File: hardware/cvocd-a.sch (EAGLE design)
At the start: 78 parts, among them IC1 6N138, IC2 LM324D, IC3 MCP4728_QUAD_DAC, IC4 REG1117, IC5 PIC16F1825SO14, IC6 74HC595D, IC7 74HC595D

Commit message: v5 pcb release candidate
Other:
- note added: "REVISION 5, 22 FEB 2018"
- note removed: "REVISION 4, 30 JAN 2018"
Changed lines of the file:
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@@
 <plain>
 <text x="59.436" y="172.212" size="3.81" layer="95">CV.OCD MIDI TO CV CONVERTER</text>
-<text x="59.944" y="166.37" size="3.81" layer="95">REVISION 4, 30 JAN 2018</text>
+<text x="59.944" y="166.37" size="3.81" layer="95">REVISION 5, 22 FEB 2018</text>
 <text x="59.944" y="160.782" size="3.81" layer="95">Jason Hotchkiss, Sixty-Four Pixels Ltd</text>
 <text x="-152.4" y="185.42" size="3.81" layer="95">POWER SUPPLY</text>
@@
 <wire x1="137.16" y1="114.3" x2="147.32" y2="114.3" width="0.1524" layer="91"/>
 <junction x="137.16" y="114.3"/>
+<junction x="147.32" y="114.3"/>
 </segment>
 </net>
@@
 <wire x1="137.16" y1="99.06" x2="147.32" y2="99.06" width="0.1524" layer="91"/>
 <junction x="137.16" y="99.06"/>
+<junction x="147.32" y="99.06"/>
 </segment>
 </net>
@@
 <wire x1="137.16" y1="83.82" x2="147.32" y2="83.82" width="0.1524" layer="91"/>
 <junction x="137.16" y="83.82"/>
+<junction x="147.32" y="83.82"/>
 </segment>
 </net>
@@
 <wire x1="137.16" y1="68.58" x2="147.32" y2="68.58" width="0.1524" layer="91"/>
 <junction x="137.16" y="68.58"/>
+<junction x="147.32" y="68.58"/>
 </segment>
 </net>
@@
 <wire x1="162.56" y1="106.68" x2="162.56" y2="114.3" width="0.1524" layer="91"/>
 <junction x="162.56" y="114.3"/>
+<junction x="157.48" y="114.3"/>
+<junction x="157.48" y="106.68"/>
 </segment>
 </net>
@@
 <wire x1="162.56" y1="91.44" x2="162.56" y2="99.06" width="0.1524" layer="91"/>
 <junction x="162.56" y="99.06"/>
+<junction x="157.48" y="99.06"/>
+<junction x="157.48" y="91.44"/>
 </segment>
 </net>
@@
 <wire x1="162.56" y1="76.2" x2="162.56" y2="83.82" width="0.1524" layer="91"/>
 <junction x="162.56" y="83.82"/>
+<junction x="157.48" y="83.82"/>
+<junction x="157.48" y="76.2"/>
 </segment>
 </net>
@@
 <wire x1="162.56" y1="60.96" x2="162.56" y2="68.58" width="0.1524" layer="91"/>
 <junction x="162.56" y="68.58"/>
-</segment>
-</net>
+<junction x="157.48" y="68.58"/>
+<junction x="157.48" y="60.96"/>
+</segment>
+</net>

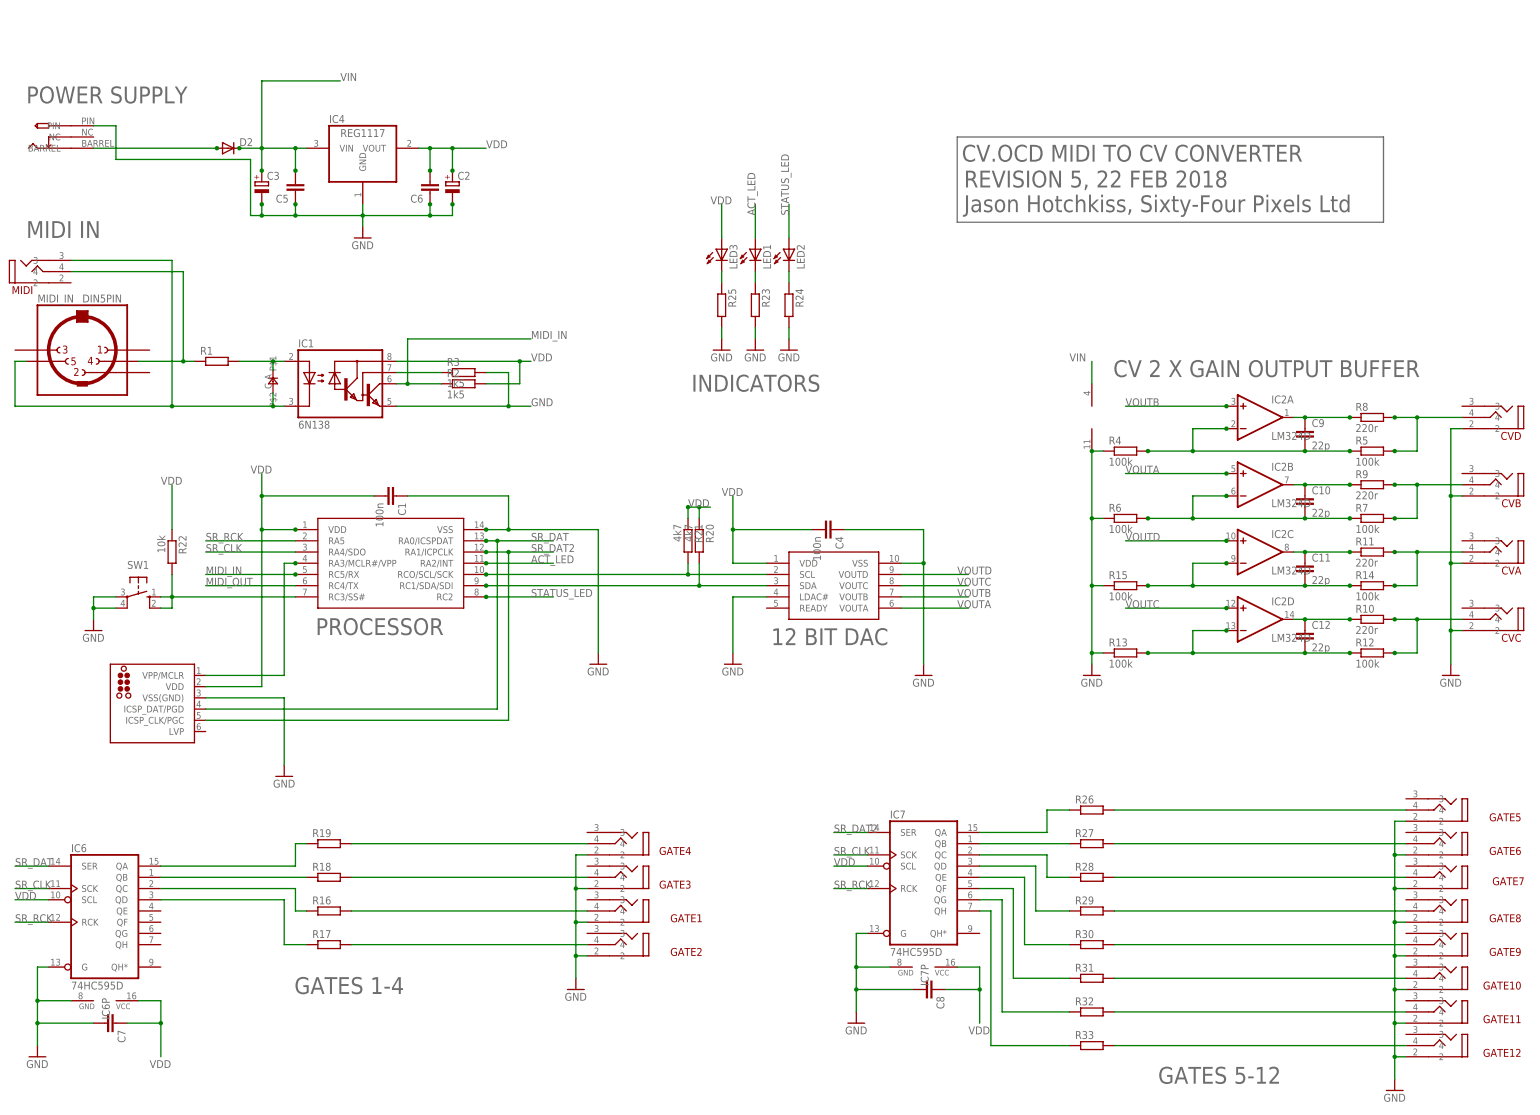
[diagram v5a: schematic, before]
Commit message: V5.1 SILK SCREEN UPDATES
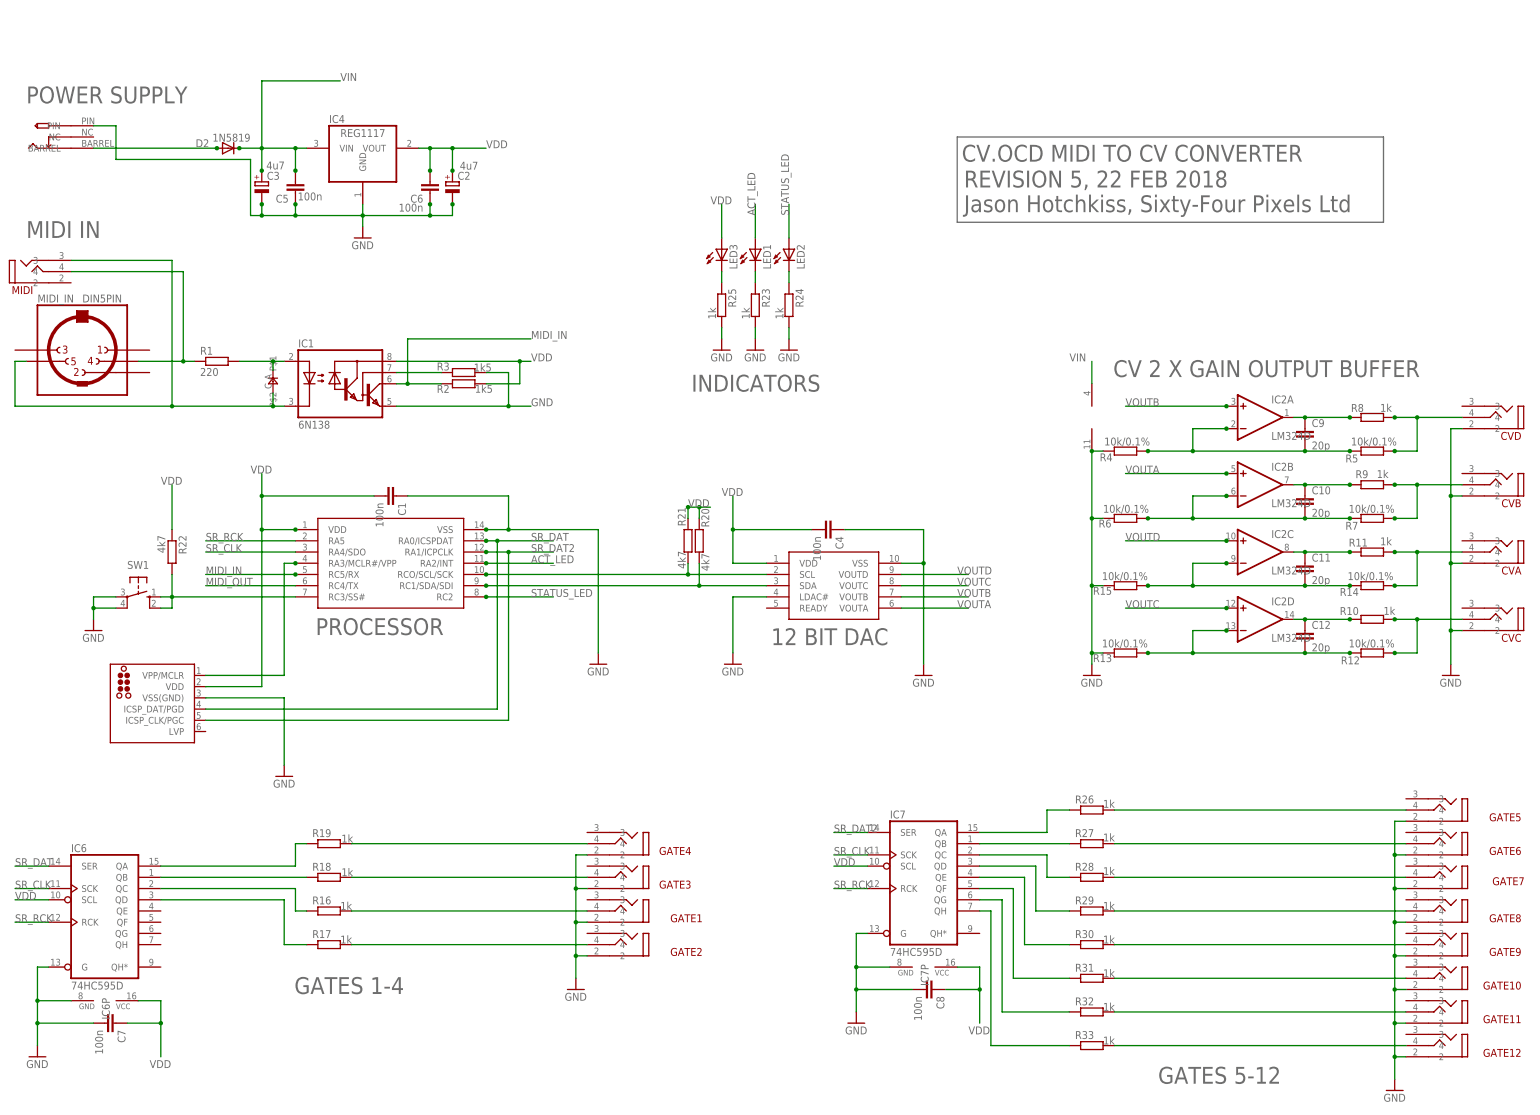
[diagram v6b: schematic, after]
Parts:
- C10, C11, C12, C9: value 22p -> 20p
- C2, C3: value (none) -> 4u7
- C5, C6, C7, C8: value (none) -> 100n
- D2: value (none) -> 1N5819
- R1: value (none) -> 220
- R10, R11, R8, R9: value 220r -> 1k
- R12, R13, R14, R15, R4, R5, R6, R7: value 100k -> 10k/0.1%
- R16, R17, R18, R19, R23, R24, R25, R26, R27, R28, R29, R30, R31, R32, R33: value (none) -> 1k
- R22: value 10k -> 4k7

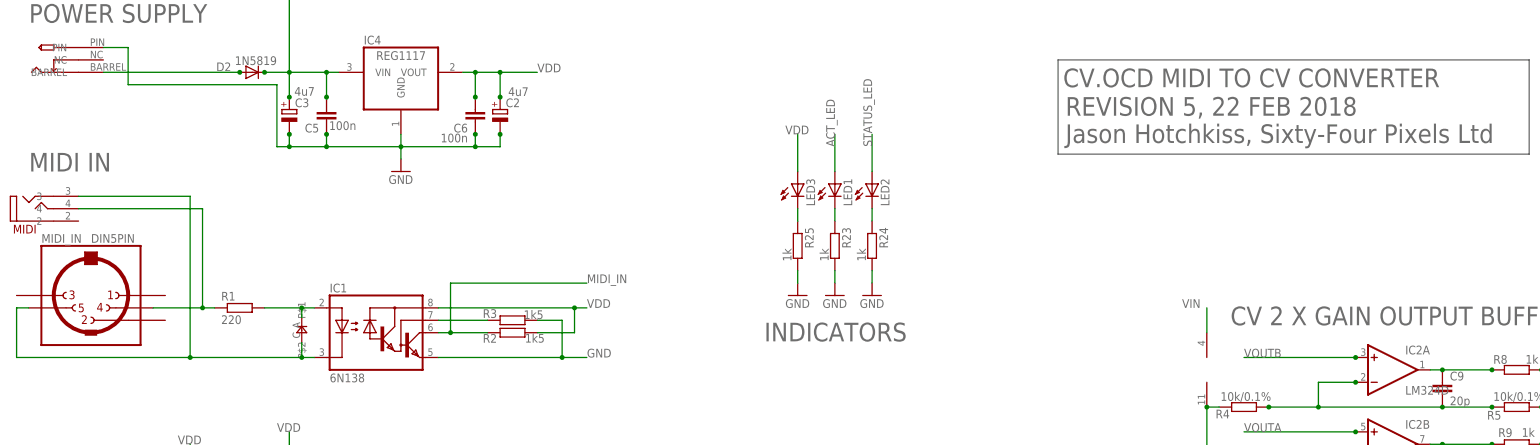
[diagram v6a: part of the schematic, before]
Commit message: V6 candidate
change polarity on mini midi in socket
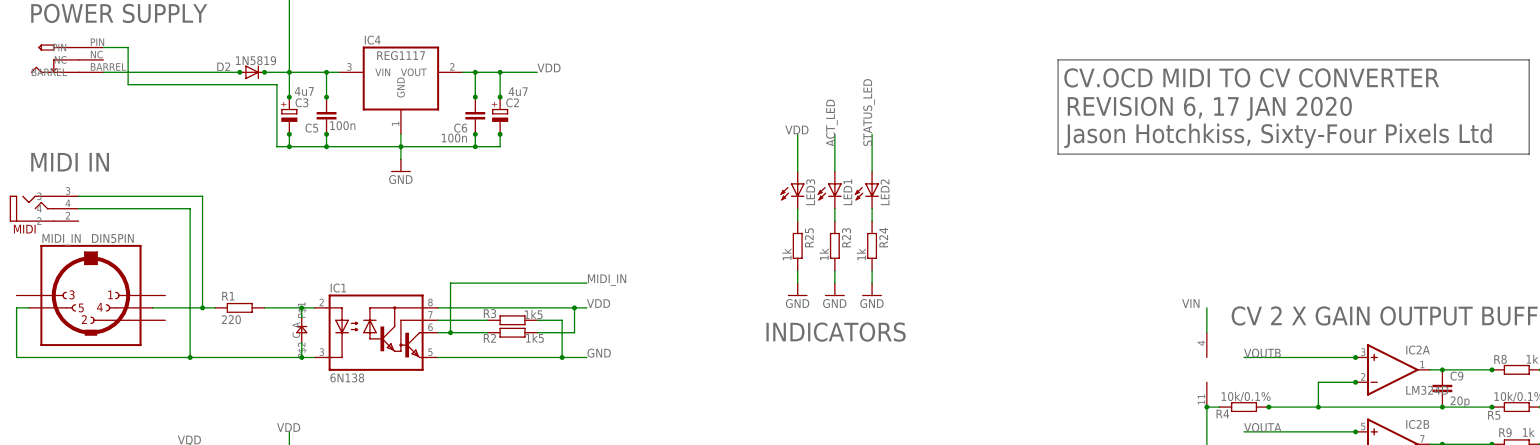
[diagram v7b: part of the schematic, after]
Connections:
- net N$29: now also MIDI.3; no longer MIDI.4
- net N$31: now also MIDI.4; no longer MIDI.3
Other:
- note added: "REVISION 6, 17 JAN 2020"
- note removed: "REVISION 5, 22 FEB 2018"
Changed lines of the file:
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@@
 <plain>
 <text x="59.436" y="172.212" size="3.81" layer="95">CV.OCD MIDI TO CV CONVERTER</text>
-<text x="59.944" y="166.37" size="3.81" layer="95">REVISION 5, 22 FEB 2018</text>
+<text x="59.944" y="166.37" size="3.81" layer="95">REVISION 6, 17 JAN 2020</text>
 <text x="59.944" y="160.782" size="3.81" layer="95">Jason Hotchkiss, Sixty-Four Pixels Ltd</text>
 <text x="-152.4" y="185.42" size="3.81" layer="95">POWER SUPPLY</text>
@@
 <pinref part="R1" gate="G$1" pin="1"/>
 <wire x1="-127" y1="127" x2="-116.84" y2="127" width="0.1524" layer="91"/>
-<pinref part="MIDI" gate="G$1" pin="4"/>
 <wire x1="-116.84" y1="127" x2="-114.3" y2="127" width="0.1524" layer="91"/>
-<wire x1="-142.24" y1="147.32" x2="-116.84" y2="147.32" width="0.1524" layer="91"/>
-<wire x1="-116.84" y1="147.32" x2="-116.84" y2="127" width="0.1524" layer="91"/>
+<wire x1="-116.84" y1="149.86" x2="-116.84" y2="127" width="0.1524" layer="91"/>
 <junction x="-116.84" y="127"/>
+<pinref part="MIDI" gate="G$1" pin="3"/>
+<wire x1="-142.24" y1="149.86" x2="-116.84" y2="149.86" width="0.1524" layer="91"/>
 </segment>
 </net>
@@
 <wire x1="-96.52" y1="119.888" x2="-96.52" y2="116.84" width="0.1524" layer="91"/>
 <junction x="-96.52" y="116.84"/>
-<pinref part="MIDI" gate="G$1" pin="3"/>
-<wire x1="-142.24" y1="149.86" x2="-119.38" y2="149.86" width="0.1524" layer="91"/>
-<wire x1="-119.38" y1="149.86" x2="-119.38" y2="116.84" width="0.1524" layer="91"/>
+<wire x1="-119.38" y1="147.32" x2="-119.38" y2="116.84" width="0.1524" layer="91"/>
 <junction x="-119.38" y="116.84"/>
-</segment>
-</net>
+<pinref part="MIDI" gate="G$1" pin="4"/>
+<wire x1="-142.24" y1="147.32" x2="-119.38" y2="147.32" width="0.1524" layer="91"/>
+</segment>
+</net>

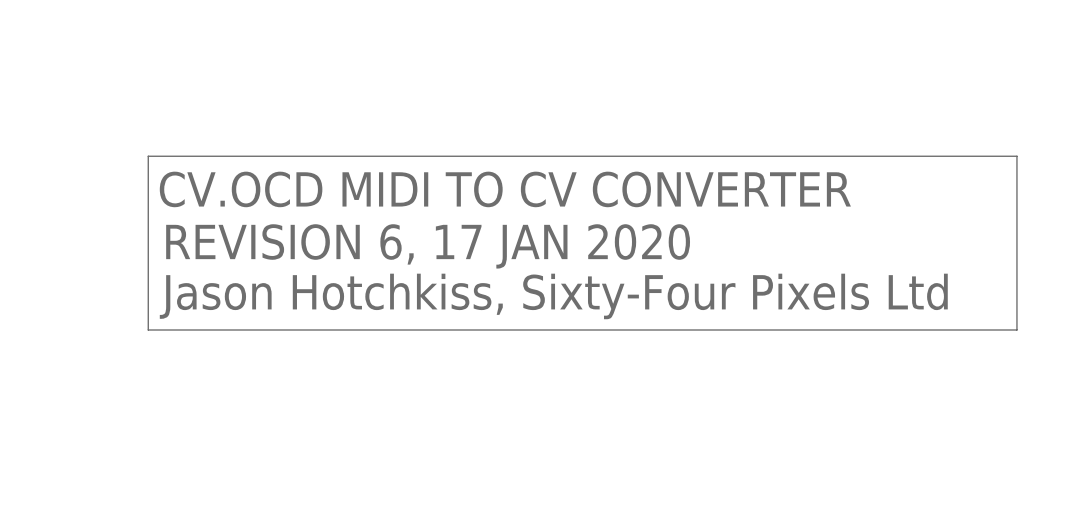
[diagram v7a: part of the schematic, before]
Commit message: REV 6A - Diode direction marking only
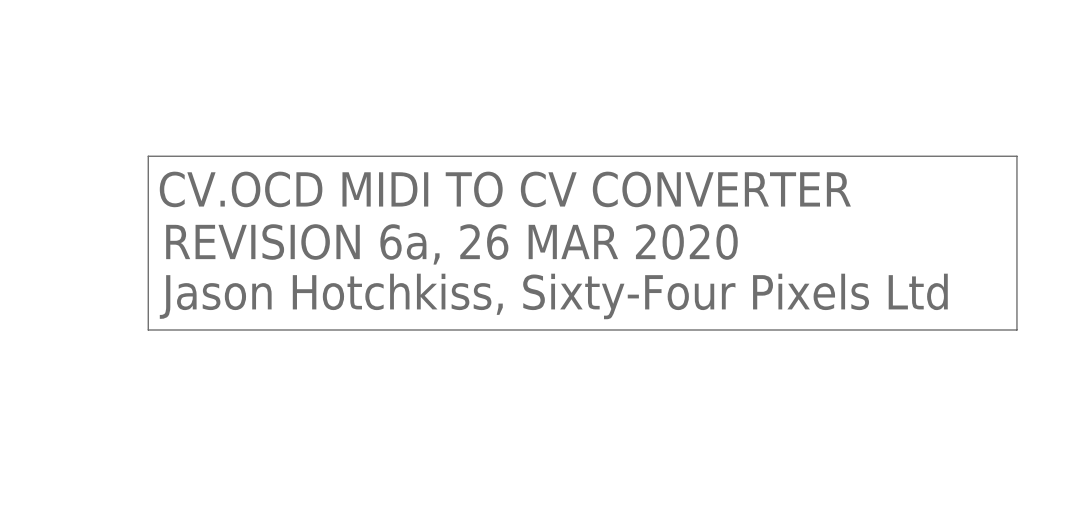
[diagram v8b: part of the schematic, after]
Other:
- note added: "REVISION 6a, 26 MAR 2020"
- note removed: "REVISION 6, 17 JAN 2020"
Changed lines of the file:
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@@
 <plain>
 <text x="59.436" y="172.212" size="3.81" layer="95">CV.OCD MIDI TO CV CONVERTER</text>
-<text x="59.944" y="166.37" size="3.81" layer="95">REVISION 6, 17 JAN 2020</text>
+<text x="59.944" y="166.37" size="3.81" layer="95">REVISION 6a, 26 MAR 2020</text>
 <text x="59.944" y="160.782" size="3.81" layer="95">Jason Hotchkiss, Sixty-Four Pixels Ltd</text>
 <text x="-152.4" y="185.42" size="3.81" layer="95">POWER SUPPLY</text>
